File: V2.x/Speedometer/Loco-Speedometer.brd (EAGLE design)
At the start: 34.6 x 14 mm, 47 parts, among them IC1 Atmega 328-P, IC2 MCP2515, IC3 A1324LLHLT, Q1 8MHz, Q2 16MHz, U1 DRV8836, U2 ST732M50RSOT23-5L_STM, U3 DRV8836, U4 DRV8836

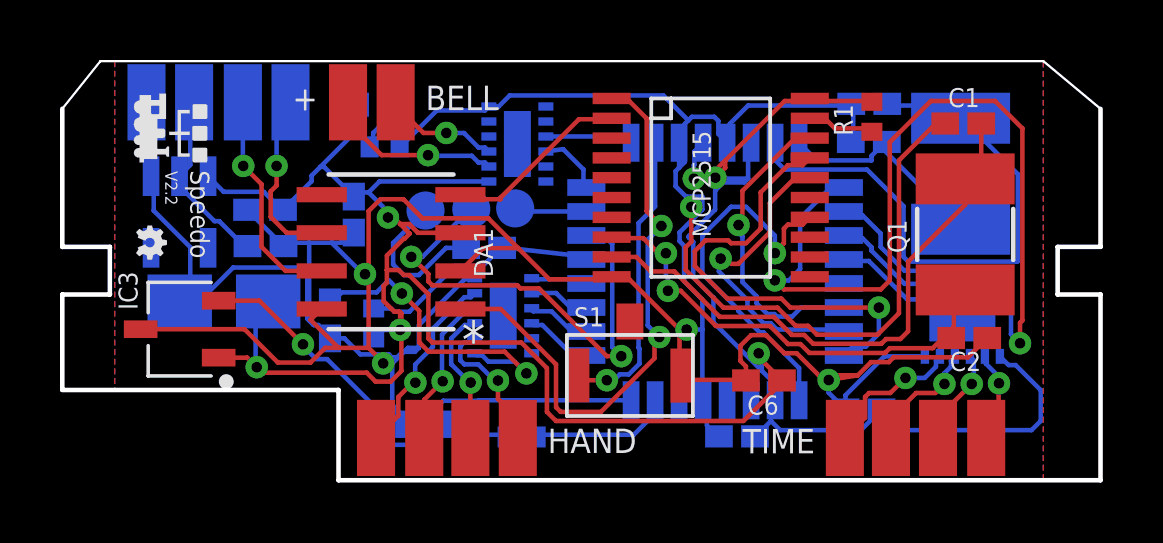
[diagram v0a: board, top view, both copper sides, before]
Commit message: Speedometer added mechanics with housing files added
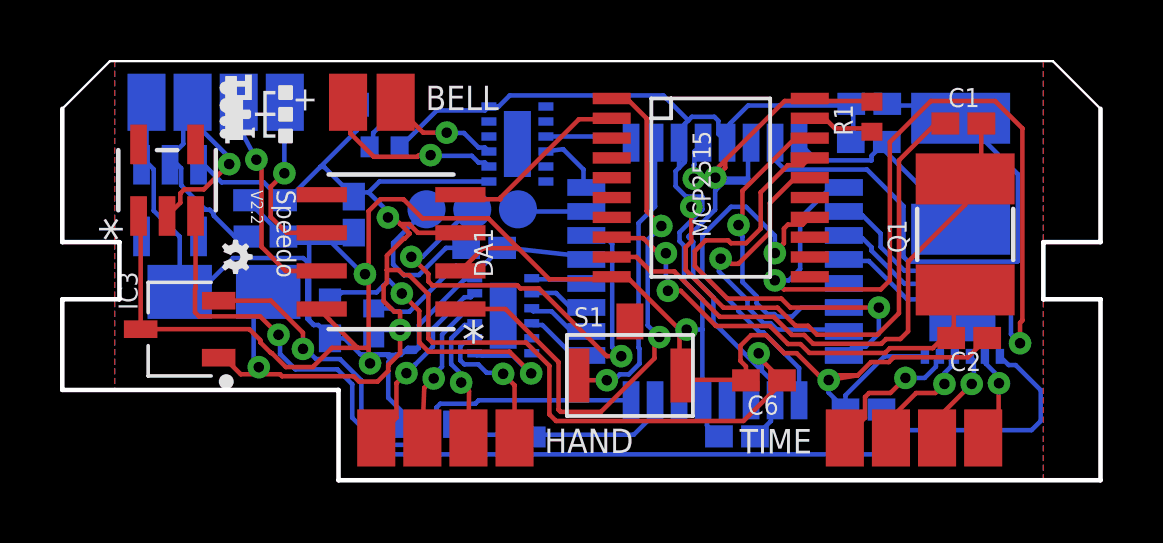
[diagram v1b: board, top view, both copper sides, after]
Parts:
- added U5: ST732M50RSOT23-5L_STM, ST732:SOT23-5L_STM
- +, +B, BELL, GND, H, HAND, L, TIME, U1-, U2+, U2-, Z1-, Z2+, Z2-: device wirepad:SMD1,27-2,54 -> wirepad:SMD1,27-1,90
- CAN: value CAN -> LED_BLUE
- moved U2 0.50 mm to (3.59, 9.48)
- moved C11 0.32 mm to (6.77, 8.28)
- moved C15 0.32 mm to (6.76, 9.49)
- moved C16 0.32 mm to (5.39, 6.44)
- moved L 0.19 mm to (7.42, 12.8)
- moved H 0.14 mm to (5.88, 12.8)
- moved HAND 0.11 mm to (15.1, 1.57)
- moved TIME 0.10 mm to (30.7, 1.57)
- moved RX 0.10 mm to (15.2, 9.19)
- moved Z1- 0.06 mm to (13.5, 1.57)
- moved Z2+ 0.06 mm to (12.0, 1.57)
- moved DTR 0.05 mm to (12.1, 9.19)
- moved +B 0.05 mm to (4.34, 12.8)
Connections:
- new net +5V: C9.1, U1.1, U5.3
- net +12V: now also U5.2
- net GND: now also U5.1
- net VCC: no longer C9.1, U1.1
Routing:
- net +5V: track 0.00 -> 38.7 mm, vias 0 -> 1
- net VCC: track 88.7 -> 76.0 mm
- net +12V: track 6.09 -> 11.9 mm, vias 0 -> 1
- net GND: track 136.0 -> 140.4 mm
- net A1: track 17.1 -> 17.6 mm
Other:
- outline, holes or cut-outs redrawn
